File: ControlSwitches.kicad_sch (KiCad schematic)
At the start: 16 parts, among them SW1 HAZARD, SW2 CRUISE_SET, SW3 CRUISE, SW4 F/R_SW, SW5 HEADLIGHT_SW, SW7 TURN_SIGNAL_SW, SW8 REGEN_SW

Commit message: finished schematic rev1
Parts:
- removed SW8: REGEN_SW, Connector_Molex:Molex_Micro-Fit_3.0_43650-0200_1x02_P3.00mm_Horizontal, symbol Switch:SW_Push
- added SW8: REGEN_SW, Connector_Molex:Molex_Micro-Fit_3.0_43650-0200_1x02_P3.00mm_Horizontal, symbol Switch:SW_SPST
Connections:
- net +3V3: now also SW4.2, SW7.2, SW8.2 (B); no longer R16.1, R17.1, R19.1, R20.1
- net GND: now also R16.1, R17.1, R19.1, R20.1; no longer SW4.2, SW7.2
- net REGEN_SW: now also SW8.1 (A)
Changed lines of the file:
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@@
     (pin "3")
-  )
-  (symbol (lib_id "power:GND") (at 190.5 93.98 0) (mirror y) (unit 1)
-    (in_bom yes) (on_board yes)
-    (property "Reference" "#PWR0126" (id 0) (at 190.5 100.33 0)
-      (effects (font (size 1.27 1.27)) hide)
-    )
-    (property "Value" "GND" (id 1) (at 190.373 98.3742 0))
-    (property "Footprint" "" (id 2) (at 190.5 93.98 0)
-      (effects (font (size 1.27 1.27)) hide)
-    )
-    (property "Datasheet" "" (id 3) (at 190.5 93.98 0)
-      (effects (font (size 1.27 1.27)) hide)
-    )
-    (pin "1")
   )
   (symbol (lib_id "power:GND") (at 53.34 148.59 0) (unit 1)
@@
     (pin "2")
   )
-  (symbol (lib_id "power:+3.3V") (at 219.71 80.01 0) (mirror y) (unit 1)
-    (in_bom yes) (on_board yes)
-    (property "Reference" "#PWR0134" (id 0) (at 219.71 83.82 0)
-      (effects (font (size 1.27 1.27)) hide)
-    )
-    (property "Value" "+3.3V" (id 1) (at 219.329 75.6158 0))
-    (property "Footprint" "" (id 2) (at 219.71 80.01 0)
-      (effects (font (size 1.27 1.27)) hide)
-    )
-    (property "Datasheet" "" (id 3) (at 219.71 80.01 0)
-      (effects (font (size 1.27 1.27)) hide)
-    )
-    (pin "1")
-  )
-  (symbol (lib_id "power:+3.3V") (at 210.82 80.01 0) (mirror y) (unit 1)
-    (in_bom yes) (on_board yes)
-    (property "Reference" "#PWR0135" (id 0) (at 210.82 83.82 0)
-      (effects (font (size 1.27 1.27)) hide)
-    )
-    (property "Value" "+3.3V" (id 1) (at 210.439 75.6158 0))
-    (property "Footprint" "" (id 2) (at 210.82 80.01 0)
-      (effects (font (size 1.27 1.27)) hide)
-    )
-    (property "Datasheet" "" (id 3) (at 210.82 80.01 0)
-      (effects (font (size 1.27 1.27)) hide)
-    )
-    (pin "1")
-  )
   (symbol (lib_id "power:GND") (at 135.89 105.41 0) (unit 1)
     (in_bom yes) (on_board yes)
@@
     )
     (pin "1")
-  )
-  (symbol (lib_id "Switch:SW_Push") (at 135.89 87.63 90) (unit 1)
-    (in_bom yes) (on_board yes)
-    (property "Reference" "SW8" (id 0) (at 142.24 85.09 90))
-    (property "Value" "REGEN_SW" (id 1) (at 142.24 87.63 90))
-    (property "Footprint" "Connector_Molex:Molex_Micro-Fit_3.0_43650-0200_1x02_P3.00mm_Horizontal" (id 2) (at 135.89 87.63 0)
-      (effects (font (size 1.27 1.27)) hide)
-    )
-    (property "Datasheet" "~" (id 3) (at 135.89 87.63 0)
-      (effects (font (size 1.27 1.27)) hide)
-    )
-    (pin "1")
-    (pin "2")
   )
   (symbol (lib_id "Device:R_US") (at 135.89 99.06 180) (unit 1)
@@
     (pin "2")
   )
-  (symbol (lib_id "power:GND") (at 190.5 124.46 0) (unit 1)
-    (in_bom yes) (on_board yes)
-    (property "Reference" "#PWR013" (id 0) (at 190.5 130.81 0)
-      (effects (font (size 1.27 1.27)) hide)
-    )
-    (property "Value" "GND" (id 1) (at 190.627 128.8542 0))
-    (property "Footprint" "" (id 2) (at 190.5 124.46 0)
-      (effects (font (size 1.27 1.27)) hide)
-    )
-    (property "Datasheet" "" (id 3) (at 190.5 124.46 0)
-      (effects (font (size 1.27 1.27)) hide)
-    )
-    (pin "1")
-  )
   (symbol (lib_id "Switch:SW_SPDT_MSM") (at 199.39 121.92 0) (mirror x) (unit 1)
     (in_bom yes) (on_board yes)
@@
     (pin "2")
   )
-  (symbol (lib_id "power:+3.3V") (at 210.82 107.95 0) (unit 1)
-    (in_bom yes) (on_board yes)
-    (property "Reference" "#PWR014" (id 0) (at 210.82 111.76 0)
-      (effects (font (size 1.27 1.27)) hide)
-    )
-    (property "Value" "+3.3V" (id 1) (at 211.201 103.5558 0))
-    (property "Footprint" "" (id 2) (at 210.82 107.95 0)
-      (effects (font (size 1.27 1.27)) hide)
-    )
-    (property "Datasheet" "" (id 3) (at 210.82 107.95 0)
-      (effects (font (size 1.27 1.27)) hide)
-    )
-    (pin "1")
-  )
-  (symbol (lib_id "power:+3.3V") (at 219.71 107.95 0) (unit 1)
-    (in_bom yes) (on_board yes)
-    (property "Reference" "#PWR015" (id 0) (at 219.71 111.76 0)
-      (effects (font (size 1.27 1.27)) hide)
-    )
-    (property "Value" "+3.3V" (id 1) (at 220.091 103.5558 0))
-    (property "Footprint" "" (id 2) (at 219.71 107.95 0)
-      (effects (font (size 1.27 1.27)) hide)
-    )
-    (property "Datasheet" "" (id 3) (at 219.71 107.95 0)
-      (effects (font (size 1.27 1.27)) hide)
-    )
-    (pin "1")
-  )
   (symbol (lib_id "power:+3.3V") (at 53.34 80.01 0) (mirror y) (unit 1)
     (in_bom yes) (on_board yes)
@@
       (effects (font (size 1.27 1.27)) hide)
     )
+    (pin "1")
+    (pin "2")
+  )
+  (symbol (lib_id "power:GND") (at 210.82 80.01 180) (unit 1)
+    (in_bom yes) (on_board yes) (fields_autoplaced)
+    (property "Reference" "#PWR0120" (id 0) (at 210.82 73.66 0)
+      (effects (font (size 1.27 1.27)) hide)
+    )
+    (property "Value" "GND" (id 1) (at 210.82 74.93 0))
+    (property "Footprint" "" (id 2) (at 210.82 80.01 0)
+      (effects (font (size 1.27 1.27)) hide)
+    )
+    (property "Datasheet" "" (id 3) (at 210.82 80.01 0)
+      (effects (font (size 1.27 1.27)) hide)
+    )
+    (pin "1")
+  )
+  (symbol (lib_id "power:GND") (at 219.71 107.95 180) (unit 1)
+    (in_bom yes) (on_board yes) (fields_autoplaced)
+    (property "Reference" "#PWR0116" (id 0) (at 219.71 101.6 0)
+      (effects (font (size 1.27 1.27)) hide)
+    )
+    (property "Value" "GND" (id 1) (at 219.71 102.87 0))
+    (property "Footprint" "" (id 2) (at 219.71 107.95 0)
+      (effects (font (size 1.27 1.27)) hide)
+    )
+    (property "Datasheet" "" (id 3) (at 219.71 107.95 0)
+      (effects (font (size 1.27 1.27)) hide)
+    )
+    (pin "1")
+  )
+  (symbol (lib_id "power:GND") (at 219.71 80.01 180) (unit 1)
+    (in_bom yes) (on_board yes) (fields_autoplaced)
+    (property "Reference" "#PWR0118" (id 0) (at 219.71 73.66 0)
+      (effects (font (size 1.27 1.27)) hide)
+    )
+    (property "Value" "GND" (id 1) (at 219.71 74.93 0))
+    (property "Footprint" "" (id 2) (at 219.71 80.01 0)
+      (effects (font (size 1.27 1.27)) hide)
+    )
+    (property "Datasheet" "" (id 3) (at 219.71 80.01 0)
+      (effects (font (size 1.27 1.27)) hide)
+    )
+    (pin "1")
+  )
+  (symbol (lib_id "power:+3.3V") (at 190.5 93.98 180) (unit 1)
+    (in_bom yes) (on_board yes) (fields_autoplaced)
+    (property "Reference" "#PWR0119" (id 0) (at 190.5 90.17 0)
+      (effects (font (size 1.27 1.27)) hide)
+    )
+    (property "Value" "+3.3V" (id 1) (at 190.5 99.06 0))
+    (property "Footprint" "" (id 2) (at 190.5 93.98 0)
+      (effects (font (size 1.27 1.27)) hide)
+    )
+    (property "Datasheet" "" (id 3) (at 190.5 93.98 0)
+      (effects (font (size 1.27 1.27)) hide)
+    )
+    (pin "1")
+  )
+  (symbol (lib_id "power:+3.3V") (at 190.5 124.46 180) (unit 1)
+    (in_bom yes) (on_board yes) (fields_autoplaced)
+    (property "Reference" "#PWR0121" (id 0) (at 190.5 120.65 0)
+      (effects (font (size 1.27 1.27)) hide)
+    )
+    (property "Value" "+3.3V" (id 1) (at 190.5 129.54 0))
+    (property "Footprint" "" (id 2) (at 190.5 124.46 0)
+      (effects (font (size 1.27 1.27)) hide)
+    )
+    (property "Datasheet" "" (id 3) (at 190.5 124.46 0)
+      (effects (font (size 1.27 1.27)) hide)
+    )
+    (pin "1")
+  )
+  (symbol (lib_id "power:GND") (at 210.82 107.95 180) (unit 1)
+    (in_bom yes) (on_board yes) (fields_autoplaced)
+    (property "Reference" "#PWR0117" (id 0) (at 210.82 101.6 0)
+      (effects (font (size 1.27 1.27)) hide)
+    )
+    (property "Value" "GND" (id 1) (at 210.82 102.87 0))
+    (property "Footprint" "" (id 2) (at 210.82 107.95 0)
+      (effects (font (size 1.27 1.27)) hide)
+    )
+    (property "Datasheet" "" (id 3) (at 210.82 107.95 0)
+      (effects (font (size 1.27 1.27)) hide)
+    )
+    (pin "1")
+  )
+  (symbol (lib_id "Switch:SW_SPST") (at 135.89 87.63 90) (unit 1)
+    (in_bom yes) (on_board yes)
+    (property "Reference" "SW8" (id 0) (at 142.24 86.36 90))
+    (property "Value" "REGEN_SW" (id 1) (at 142.24 88.9 90))
+    (property "Footprint" "Connector_Molex:Molex_Micro-Fit_3.0_43650-0200_1x02_P3.00mm_Horizontal" (id 2) (at 135.89 87.63 0)
+      (effects (font (size 1.27 1.27)) hide)
+    )
+    (property "Datasheet" "~" (id 3) (at 135.89 87.63 0)
+      (effects (font (size 1.27 1.27)) hide)
+    )

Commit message: redo schematic
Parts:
- removed R13, R16, R17, R21: 10k, Resistor_SMD:R_0805_2012Metric, symbol Device:R_US
- removed SW1: HAZARD, Connector_Molex:Molex_Micro-Fit_3.0_43650-0200_1x02_P3.00mm_Horizontal, symbol Switch:SW_SPST
- removed SW5: HEADLIGHT_SW, Connector_Molex:Molex_Micro-Fit_3.0_43650-0200_1x02_P3.00mm_Horizontal, symbol Switch:SW_SPST
- removed SW7: TURN_SIGNAL_SW, Connector_Molex:Molex_Micro-Fit_3.0_43650-0300_1x03_P3.00mm_Horizontal, symbol Switch:SW_SPDT_MSM
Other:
- moved on the sheet: R14, R15, R9, SW2, SW3, SW8

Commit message: added todo
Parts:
- renumbered R14 to R3, R15 to R4, R9 to R5, R19 to R6, R20 to R7, SW2 to SW1, SW3 to SW2, SW8 to SW3
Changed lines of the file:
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@@
   (symbol (lib_id "Switch:SW_Push") (at 55.245 111.76 90) (unit 1)
     (in_bom yes) (on_board yes)
-    (property "Reference" "SW2" (id 0) (at 61.595 109.22 90))
+    (property "Reference" "SW1" (id 0) (at 61.595 109.22 90))
     (property "Value" "CRUISE_SET" (id 1) (at 61.1886 111.76 90))
     (property "Footprint" "Connector_Molex:Molex_Micro-Fit_3.0_43650-0200_1x02_P3.00mm_Horizontal" (id 2) (at 55.245 111.76 0)
@@
   (symbol (lib_id "Device:R_US") (at 55.245 123.19 0) (unit 1)
     (in_bom yes) (on_board yes)
-    (property "Reference" "R14" (id 0) (at 59.055 121.92 0))
+    (property "Reference" "R3" (id 0) (at 59.055 121.92 0))
     (property "Value" "10k" (id 1) (at 59.055 124.46 0))
     (property "Footprint" "Resistor_SMD:R_0805_2012Metric" (id 2) (at 56.261 123.444 90)
@@
   (symbol (lib_id "Switch:SW_Push") (at 97.155 111.76 90) (unit 1)
     (in_bom yes) (on_board yes)
-    (property "Reference" "SW3" (id 0) (at 102.235 109.22 90))
+    (property "Reference" "SW2" (id 0) (at 102.235 109.22 90))
     (property "Value" "CRUISE" (id 1) (at 102.235 111.76 90))
     (property "Footprint" "Connector_Molex:Molex_Micro-Fit_3.0_43650-0200_1x02_P3.00mm_Horizontal" (id 2) (at 97.155 111.76 0)
@@
   (symbol (lib_id "Device:R_US") (at 97.155 123.19 180) (unit 1)
     (in_bom yes) (on_board yes)
-    (property "Reference" "R15" (id 0) (at 100.965 121.92 0))
+    (property "Reference" "R4" (id 0) (at 100.965 121.92 0))
     (property "Value" "10k" (id 1) (at 100.965 124.46 0))
     (property "Footprint" "Resistor_SMD:R_0805_2012Metric" (id 2) (at 96.139 122.936 90)
@@
   (symbol (lib_id "Device:R_US") (at 137.795 123.19 180) (unit 1)
     (in_bom yes) (on_board yes)
-    (property "Reference" "R9" (id 0) (at 141.605 121.92 0))
+    (property "Reference" "R5" (id 0) (at 141.605 121.92 0))
     (property "Value" "10k" (id 1) (at 141.605 124.46 0))
     (property "Footprint" "Resistor_SMD:R_0805_2012Metric" (id 2) (at 136.779 122.936 90)
@@
   (symbol (lib_id "Device:R_US") (at 210.82 111.76 0) (unit 1)
     (in_bom yes) (on_board yes)
-    (property "Reference" "R19" (id 0) (at 212.5472 110.5916 0)
+    (property "Reference" "R6" (id 0) (at 212.5472 110.5916 0)
       (effects (font (size 1.27 1.27)) (justify left))
     )
@@
   (symbol (lib_id "Device:R_US") (at 219.71 111.76 0) (unit 1)
     (in_bom yes) (on_board yes)
-    (property "Reference" "R20" (id 0) (at 221.4372 110.5916 0)
+    (property "Reference" "R7" (id 0) (at 221.4372 110.5916 0)
       (effects (font (size 1.27 1.27)) (justify left))
     )
@@
   (symbol (lib_id "Switch:SW_SPST") (at 137.795 111.76 90) (unit 1)
     (in_bom yes) (on_board yes)
-    (property "Reference" "SW8" (id 0) (at 144.145 110.49 90))
+    (property "Reference" "SW3" (id 0) (at 144.145 110.49 90))
     (property "Value" "REGEN_SW" (id 1) (at 144.145 113.03 90))
     (property "Footprint" "Connector_Molex:Molex_Micro-Fit_3.0_43650-0200_1x02_P3.00mm_Horizontal" (id 2) (at 137.795 111.76 0)

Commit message: added comments
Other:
- note added: "Add Caps || Resistors"
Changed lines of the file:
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@@
     (stroke (width 0) (type default) (color 0 0 0 0))
+  )
+  (text "Add Caps || Resistors" (at 72.39 140.97 0)
+    (effects (font (size 1.27 1.27)) (justify left bottom))
   )
   (text "Does this work? Or should there be no pull down resistor\nand GNDPWR and it just floats when not connected? Or \ndoes it need to be SPDT?"

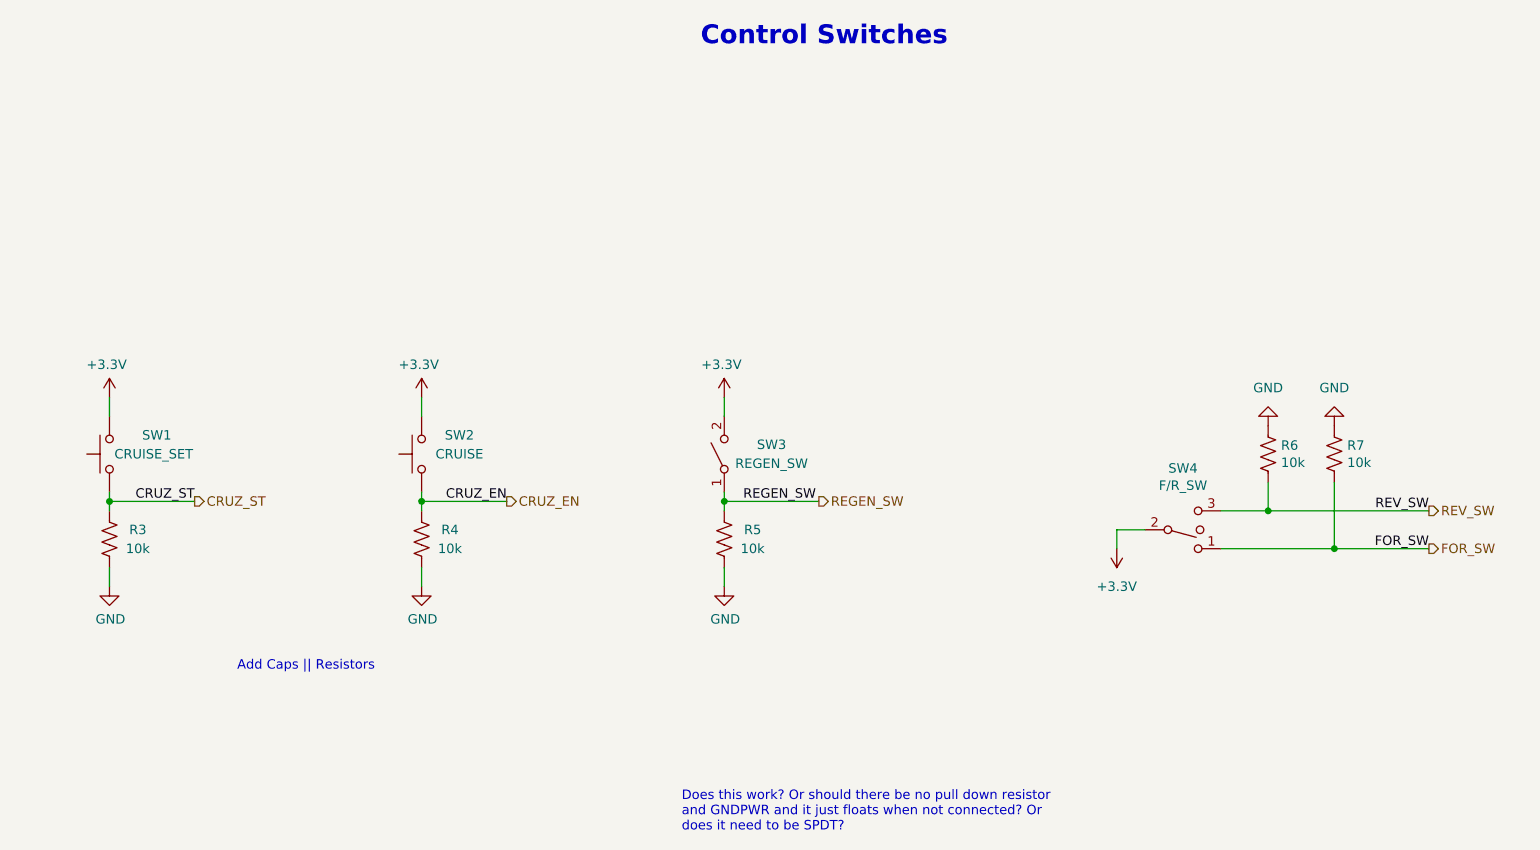
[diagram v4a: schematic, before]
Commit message: added capacitors to the switches, no-pop resistors to the light ports, added ports for internal indicator lights
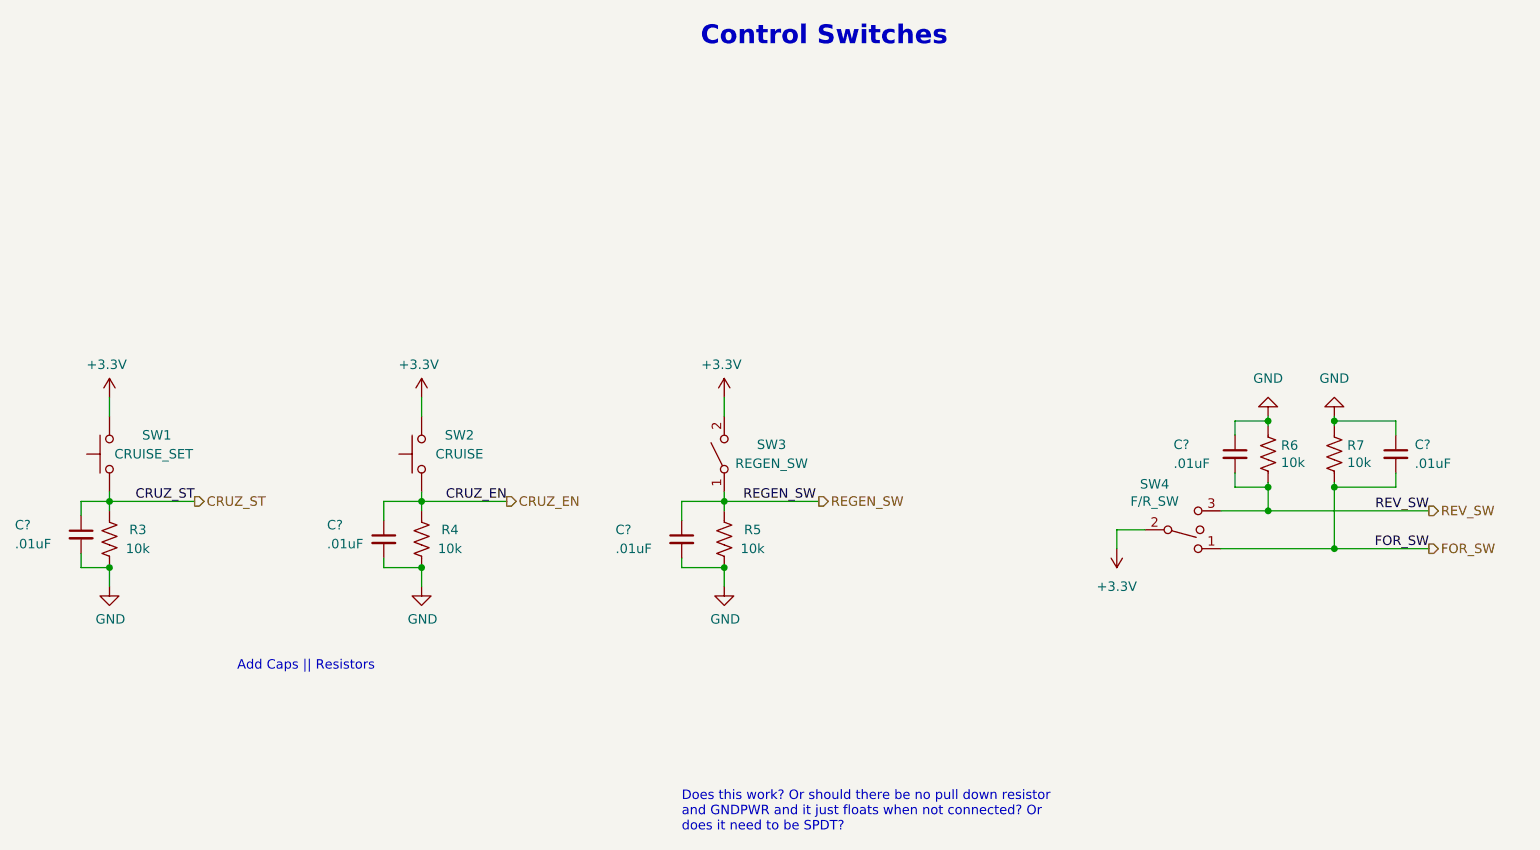
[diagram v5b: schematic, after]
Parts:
- added C? (x5): .01uF, symbol Device:C_Small
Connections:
- net CRUZ_EN: now also C?.1
- net CRUZ_ST: now also C?.1
- net FOR_SW: now also C?.2
- net GND: now also C?.1, C?.1, C?.2, C?.2, C?.2
- net REGEN_SW: now also C?.1
- net REV_SW: now also C?.2
